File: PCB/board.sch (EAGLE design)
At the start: 33 parts, among them IC2 LM340MP-05, J1 DCJ0202, J2 DCJ0202, Q1 CRYSTAL_16MHZ_SMD, U1 MLX90614_, U2 MMA8451

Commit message: Nothing
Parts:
- added C10, C11: 0.1uF, rcl:C-EUC0805
- added R7: 10K, rcl:R-EU_R0805
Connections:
- new net INT1: U2.INT1
- new net INT2: U2.INT2
- new net N$40: C11.1, U2.BYP
- new net SA0: R7.1, U2.SA0
- new net SCL_3.3V: U2.SCL
- new net SDA_3.3V: U2.SDA
- net +3V3: now also C10.1, R7.2, U2.VDD, U2.VDDIO
- net GND: now also C10.2, C11.2, U2.GND
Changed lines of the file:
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@@
 <?xml version="1.0" encoding="utf-8"?>
 <!DOCTYPE eagle SYSTEM "eagle.dtd">
-<eagle version="9.4.2">
+<eagle version="9.5.1">
 <drawing>
 <settings>
-<setting alwaysvectorfont="no"/>
+<setting alwaysvectorfont="yes"/>
 <setting verticaltext="up"/>
 </settings>
@@
 <part name="+3V4" library="supply1" library_urn="urn:adsk.eagle:library:371" deviceset="+3V3" device=""/>
 <part name="U2" library="microbuilder" deviceset="ACCEL_MMA845X" device="" value="MMA8451"/>
+<part name="+3V5" library="supply1" library_urn="urn:adsk.eagle:library:371" deviceset="+3V3" device=""/>
+<part name="C10" library="rcl" library_urn="urn:adsk.eagle:library:334" deviceset="C-EU" device="C0805" package3d_urn="urn:adsk.eagle:package:23617/2" value="0.1uF"/>
+<part name="GND16" library="supply1" library_urn="urn:adsk.eagle:library:371" deviceset="GND" device=""/>
+<part name="R7" library="rcl" library_urn="urn:adsk.eagle:library:334" deviceset="R-EU_" device="R0805" package3d_urn="urn:adsk.eagle:package:23553/2" value="10K"/>
+<part name="+3V6" library="supply1" library_urn="urn:adsk.eagle:library:371" deviceset="+3V3" device=""/>
+<part name="C11" library="rcl" library_urn="urn:adsk.eagle:library:334" deviceset="C-EU" device="C0805" package3d_urn="urn:adsk.eagle:package:23617/2" value="0.1uF"/>
+<part name="GND17" library="supply1" library_urn="urn:adsk.eagle:library:371" deviceset="GND" device=""/>
 </parts>
 <sheets>
@@
 <attribute name="VALUE" x="73.66" y="25.4" size="1.27" layer="96"/>
 </instance>
+<instance part="+3V5" gate="G$1" x="43.18" y="83.82" smashed="yes">
+<attribute name="VALUE" x="40.64" y="78.74" size="1.778" layer="96" rot="R90"/>
+</instance>
+<instance part="C10" gate="G$1" x="43.18" y="71.12" smashed="yes">
+<attribute name="NAME" x="40.259" y="67.564" size="1.778" layer="95" rot="R90"/>
+<attribute name="VALUE" x="47.879" y="67.564" size="1.778" layer="96" rot="R90"/>
+</instance>
+<instance part="GND16" gate="1" x="43.18" y="58.42" smashed="yes">
+<attribute name="VALUE" x="40.64" y="55.88" size="1.778" layer="96"/>
+</instance>
+<instance part="R7" gate="G$1" x="22.86" y="60.96" smashed="yes" rot="R90">
+<attribute name="NAME" x="21.3614" y="57.15" size="1.778" layer="95" rot="R90"/>
+<attribute name="VALUE" x="26.162" y="57.15" size="1.778" layer="96" rot="R90"/>
+</instance>
+<instance part="+3V6" gate="G$1" x="22.86" y="71.12" smashed="yes">
+<attribute name="VALUE" x="20.32" y="66.04" size="1.778" layer="96" rot="R90"/>
+</instance>
+<instance part="C11" gate="G$1" x="60.96" y="33.02" smashed="yes">
+<attribute name="NAME" x="58.039" y="29.464" size="1.778" layer="95" rot="R90"/>
+<attribute name="VALUE" x="65.659" y="29.464" size="1.778" layer="96" rot="R90"/>
+</instance>
+<instance part="GND17" gate="1" x="60.96" y="22.86" smashed="yes">
+<attribute name="VALUE" x="58.42" y="20.32" size="1.778" layer="96"/>
+</instance>
 </instances>
 <busses>
 </busses>
 <nets>
+<net name="+3V3" class="0">
+<segment>
+<pinref part="U2" gate="G$1" pin="VDDIO"/>
+<wire x1="71.12" y1="66.04" x2="68.58" y2="66.04" width="0.1524" layer="91"/>
+<wire x1="68.58" y1="66.04" x2="68.58" y2="68.58" width="0.1524" layer="91"/>
+<pinref part="U2" gate="G$1" pin="VDD"/>
+<wire x1="68.58" y1="68.58" x2="71.12" y2="68.58" width="0.1524" layer="91"/>
+<wire x1="68.58" y1="68.58" x2="68.58" y2="76.2" width="0.1524" layer="91"/>
+<junction x="68.58" y="68.58"/>
+<wire x1="68.58" y1="76.2" x2="43.18" y2="76.2" width="0.1524" layer="91"/>
+<pinref part="+3V5" gate="G$1" pin="+3V3"/>
+<wire x1="43.18" y1="76.2" x2="43.18" y2="81.28" width="0.1524" layer="91"/>
+<pinref part="C10" gate="G$1" pin="1"/>
+<wire x1="43.18" y1="76.2" x2="43.18" y2="73.66" width="0.1524" layer="91"/>
+<junction x="43.18" y="76.2"/>
+</segment>
+<segment>
+<pinref part="+3V6" gate="G$1" pin="+3V3"/>
+<pinref part="R7" gate="G$1" pin="2"/>
+<wire x1="22.86" y1="68.58" x2="22.86" y2="66.04" width="0.1524" layer="91"/>
+</segment>
+</net>
+<net name="GND" class="0">
+<segment>
+<pinref part="C10" gate="G$1" pin="2"/>
+<wire x1="43.18" y1="66.04" x2="43.18" y2="63.5" width="0.1524" layer="91"/>
+<pinref part="U2" gate="G$1" pin="GND"/>
+<wire x1="43.18" y1="63.5" x2="71.12" y2="63.5" width="0.1524" layer="91"/>
+<wire x1="43.18" y1="63.5" x2="43.18" y2="60.96" width="0.1524" layer="91"/>
+<junction x="43.18" y="63.5"/>
+<pinref part="GND16" gate="1" pin="GND"/>
+</segment>
+<segment>
+<pinref part="GND17" gate="1" pin="GND"/>
+<pinref part="C11" gate="G$1" pin="2"/>
+<wire x1="60.96" y1="25.4" x2="60.96" y2="27.94" width="0.1524" layer="91"/>
+</segment>
+</net>
+<net name="SCL_3.3V" class="0">
+<segment>
+<pinref part="U2" gate="G$1" pin="SCL"/>
+<wire x1="71.12" y1="58.42" x2="60.96" y2="58.42" width="0.1524" layer="91"/>
+<label x="60.96" y="58.42" size="1.778" layer="95"/>
+</segment>
+</net>
+<net name="SDA_3.3V" class="0">
+<segment>
+<pinref part="U2" gate="G$1" pin="SDA"/>
+<wire x1="71.12" y1="55.88" x2="60.96" y2="55.88" width="0.1524" layer="91"/>
+<label x="60.96" y="55.88" size="1.778" layer="95"/>
+</segment>
+</net>
+<net name="SA0" class="0">
+<segment>
+<pinref part="U2" gate="G$1" pin="SA0"/>
+<wire x1="71.12" y1="53.34" x2="22.86" y2="53.34" width="0.1524" layer="91"/>
+<wire x1="22.86" y1="53.34" x2="22.86" y2="55.88" width="0.1524" layer="91"/>
+<label x="60.96" y="53.34" size="1.778" layer="95"/>
+<pinref part="R7" gate="G$1" pin="1"/>
+</segment>
+</net>
+<net name="INT1" class="0">
+<segment>
+<pinref part="U2" gate="G$1" pin="INT1"/>
+<wire x1="71.12" y1="48.26" x2="60.96" y2="48.26" width="0.1524" layer="91"/>
+<label x="60.96" y="48.26" size="1.778" layer="95"/>
+</segment>
+</net>
+<net name="INT2" class="0">
+<segment>
+<pinref part="U2" gate="G$1" pin="INT2"/>
+<wire x1="71.12" y1="45.72" x2="60.96" y2="45.72" width="0.1524" layer="91"/>
+<label x="60.96" y="45.72" size="1.778" layer="95"/>
+</segment>
+</net>
+<net name="N$40" class="0">
+<segment>
+<pinref part="U2" gate="G$1" pin="BYP"/>
+<wire x1="71.12" y1="40.64" x2="60.96" y2="40.64" width="0.1524" layer="91"/>
+<wire x1="60.96" y1="40.64" x2="60.96" y2="35.56" width="0.1524" layer="91"/>
+<pinref part="C11" gate="G$1" pin="1"/>
+</segment>
+</net>
 </nets>
 </sheet>

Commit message: updated PCB with new LDO and PCB footprint
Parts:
- removed C10, C11: 0.1uF, rcl:C-EUC0805
- removed C9: 100nF, rcl:C-EUC0603
- removed J2: DCJ0202, con-jack:DCJ0202
- removed R4, R5: 10k, rcl:R-US_R0603
- removed R7: 10K, rcl:R-EU_R0805
- removed SV6: (no value), con-lstb:MA04-1
- removed U1: MLX90614_, SparkFun:MLX90614_
- removed U2: MMA8451, microbuilder:ACCEL_MMA845X
- C7: value 220nF -> 0.33uF
- C8: value 100nF -> 10uF
- IC1: value (none) -> MEGA1284P-SQUARE; device 1284p:MEGA1284P -> 1284p:MEGA1284P-SQUARE
- IC2: value LM340MP-05 -> MC33269D-3.3; device linear:LM340MP-05 -> linear:MC33269D-3.3
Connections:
- removed net INT1: U2.INT1
- removed net INT2: U2.INT2
- removed net N$21: R4.1, U1.PWM/SDA
- removed net N$22: R5.1, U1.SCL/VZ
- removed net N$36: C7.1, IC2.VI, J2.1
- removed net N$40: C11.1, U2.BYP
- removed net SA0: R7.1, U2.SA0
- removed net SCL_3.3V: U2.SCL
- removed net SDA_3.3V: U2.SDA
- net +3V3: now also R6.2; no longer C10.1, C9.1, R4.2, R5.2, R7.2, SV6.3, U1.VDD, U2.VDD, U2.VDDIO
- net +5V: now also C7.1, IC2.VI; no longer R6.2
- net GND: now also IC2.ADJ; no longer C10.2, C11.2, C9.2, IC2.GND, J2.2, J2.3, SV6.4, U1.VSS, U2.GND
- net SCL: no longer SV6.1
- net SDA: no longer SV6.2

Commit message: Added Op-Amp for peltier control and MOSFET for hot end cartridge heater control
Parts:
- added Q2: BUZ10, transistor-fet:BUZ10
- added U1: OPA564AIDWD, myLibrary:OPA564AIDWD
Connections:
- new net +12V: Q2.D
- new net G_3V: Q2.G
- net GND: now also Q2.S
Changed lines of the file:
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@@
 <part name="C8" library="rcl" library_urn="urn:adsk.eagle:library:334" deviceset="C-EU" device="C0805" package3d_urn="urn:adsk.eagle:package:23617/2" value="10uF"/>
 <part name="+3V1" library="supply1" library_urn="urn:adsk.eagle:library:371" deviceset="+3V3" device=""/>
+<part name="U1" library="myLibrary" deviceset="OPA564AIDWD" device=""/>
+<part name="Q2" library="transistor-fet" library_urn="urn:adsk.eagle:library:396" deviceset="BUZ10" device="" package3d_urn="urn:adsk.eagle:package:28520/1"/>
+<part name="GND11" library="supply1" library_urn="urn:adsk.eagle:library:371" deviceset="GND" device=""/>
 </parts>
 <sheets>
@@
 <instance part="+3V1" gate="G$1" x="137.16" y="40.64" smashed="yes">
 <attribute name="VALUE" x="134.62" y="35.56" size="1.778" layer="96" rot="R90"/>
+</instance>
+<instance part="U1" gate="A" x="38.1" y="27.94" smashed="yes">
+<attribute name="NAME" x="66.3956" y="37.0586" size="2.0828" layer="95" ratio="6" rot="SR0"/>
+<attribute name="VALUE" x="65.7606" y="34.5186" size="2.0828" layer="96" ratio="6" rot="SR0"/>
 </instance>
 </instances>
@@
 <attribute name="NAME" x="166.37" y="70.358" size="1.778" layer="95" rot="R180"/>
 </instance>
+<instance part="Q2" gate="G$1" x="190.5" y="104.14" smashed="yes">
+<attribute name="VALUE" x="179.07" y="104.14" size="1.778" layer="96"/>
+<attribute name="NAME" x="179.07" y="106.68" size="1.778" layer="95"/>
+</instance>
+<instance part="GND11" gate="1" x="195.58" y="91.44" smashed="yes">
+<attribute name="VALUE" x="193.04" y="88.9" size="1.778" layer="96"/>
+</instance>
 </instances>
 <busses>
@@
 <pinref part="GND10" gate="1" pin="GND"/>
 <wire x1="195.58" y1="25.4" x2="195.58" y2="20.32" width="0.1524" layer="91"/>
+</segment>
+<segment>
+<pinref part="Q2" gate="G$1" pin="S"/>
+<wire x1="195.58" y1="101.6" x2="195.58" y2="93.98" width="0.1524" layer="91"/>
+<pinref part="GND11" gate="1" pin="GND"/>
 </segment>
 </net>
@@
 </segment>
 </net>
+<net name="+12V" class="0">
+<segment>
+<pinref part="Q2" gate="G$1" pin="D"/>
+<wire x1="195.58" y1="106.68" x2="200.66" y2="106.68" width="0.1524" layer="91"/>
+<label x="200.66" y="106.68" size="1.778" layer="95"/>
+</segment>
+</net>
+<net name="G_3V" class="0">
+<segment>
+<pinref part="Q2" gate="G$1" pin="G"/>
+<wire x1="185.42" y1="101.6" x2="177.8" y2="101.6" width="0.1524" layer="91"/>
+<label x="177.8" y="101.6" size="1.778" layer="95"/>
+</segment>
+</net>

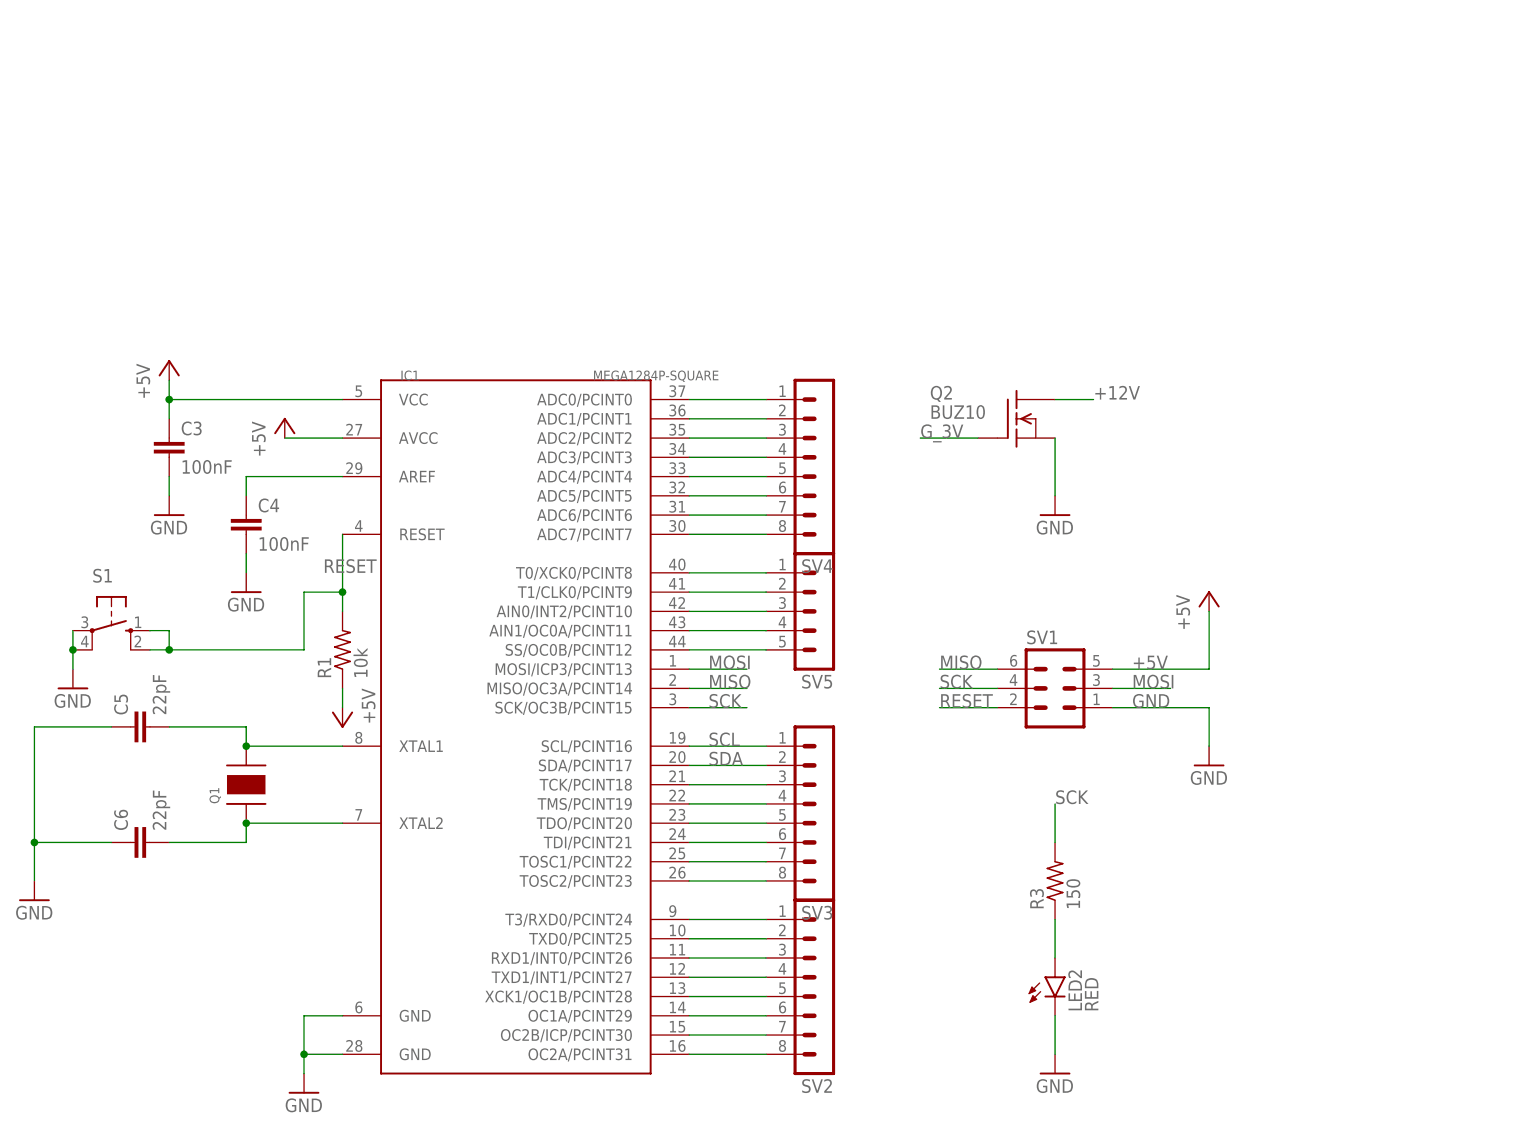
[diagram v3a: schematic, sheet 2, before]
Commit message: Added MOSFET for peltier control
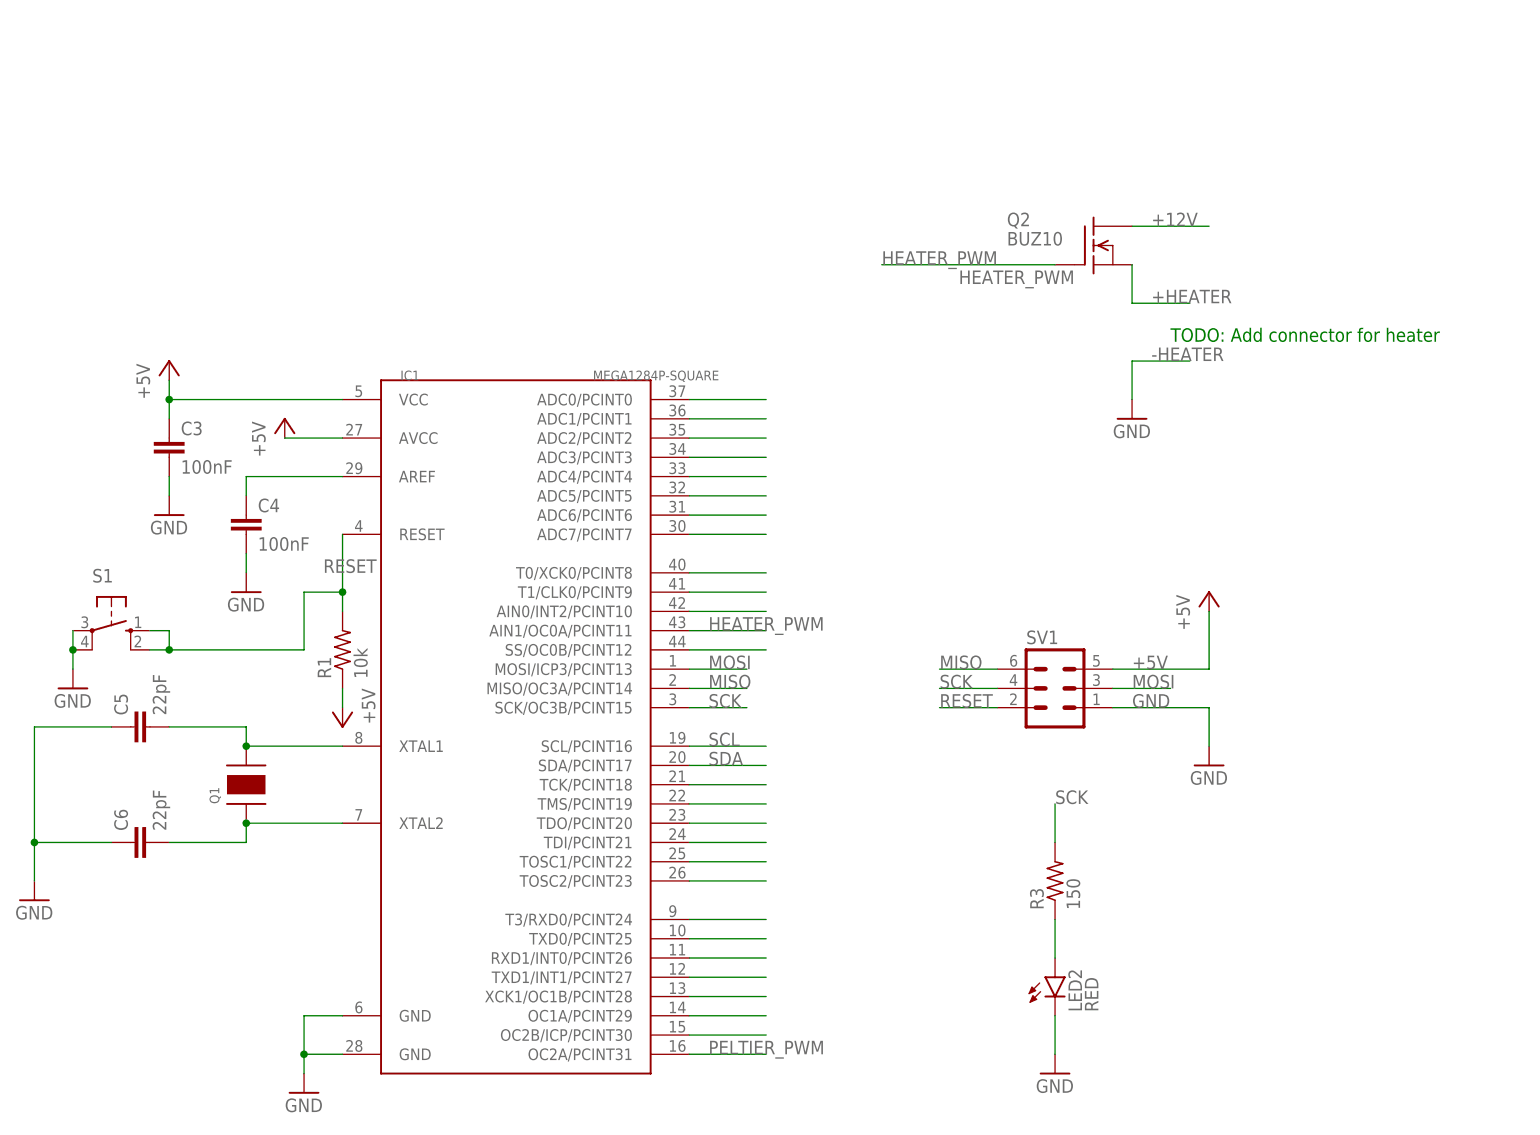
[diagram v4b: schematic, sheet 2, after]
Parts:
- removed SV2, SV3, SV4: (no value), con-lstb:MA08-1
- removed SV5: (no value), con-lstb:MA05-1
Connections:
- removed net G_3V: Q2.G
- removed net N$34: IC1.AIN1/OC0A/PCINT11, SV5.4
- removed net N$7: IC1.OC2A/PCINT31, SV2.8
- new net +HEATER: Q2.S
- new net HEATER_PWM: IC1.AIN1/OC0A/PCINT11, Q2.G
- new net PELTIER_PWM: IC1.OC2A/PCINT31
- net GND: no longer Q2.S
- net N$10: no longer SV2.5
- net N$11: no longer SV2.4
- net N$12: no longer SV2.3
- net N$13: no longer SV2.2
- net N$14: no longer SV2.1
- net N$15: no longer SV3.8
- net N$16: no longer SV3.7
- net N$17: no longer SV3.6
- net N$18: no longer SV3.5
- net N$19: no longer SV3.4
- net N$20: no longer SV3.3
- net N$23: no longer SV4.1
- net N$24: no longer SV4.2
- net N$25: no longer SV4.3
- net N$26: no longer SV4.4
- net N$27: no longer SV4.5
- net N$28: no longer SV4.6
- net N$29: no longer SV4.7
- net N$30: no longer SV4.8
- net N$31: no longer SV5.1
- net N$32: no longer SV5.2
- net N$33: no longer SV5.3
- net N$35: no longer SV5.5
- net N$8: no longer SV2.7
- net N$9: no longer SV2.6
- net SCL: no longer SV3.1
- net SDA: no longer SV3.2
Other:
- note added: "TODO: Add connector for heater"
- moved on the sheet: Q2
